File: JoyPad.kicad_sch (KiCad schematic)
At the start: 0 parts

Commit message: Adding the MCU, OLED Screen, Rotary Encoder, and switches to the sch (not done)
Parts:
- added D1, D2, D3, D4, D5, D6: (no value), symbol ScottoKeebs:Placeholder_Diode
- added J1: OLED_128x32, ScottoKeebs_Components:OLED_128x32, symbol ScottoKeebs:OLED_128x32
- added S1, S2, S3, S4, S5, S6: (no value), symbol ScottoKeebs:Placeholder_Keyswitch
- added SW1: RotaryEncoder_Switch, symbol Device:RotaryEncoder_Switch
- added U1: MCU_Seeed_XIAO_RP2040, symbol ScottoKeebs:MCU_Seeed_XIAO_RP2040
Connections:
- new net: D2.2 (A), S2.2
- new net: D6.2 (A), S6.2
- new net: D5.2 (A), S5.2
- new net: D3.2 (A), S3.2
- new net: D4.2 (A), S4.2
- new net: D1.2 (A), S1.2
- new net 5V: J1.2 (VCC), U1.14 (5V)
- new net Col 0: S1.1, S4.1, U1.3 (PA10_A2_D2)
- new net Col 1: S2.1, S5.1, U1.4 (PA11_A3_D3)
- new net Col 2: S3.1, S6.1, U1.11 (PA6_A10_D10_MOSI)
- new net GND: J1.1 (GND), SW1.C, U1.13 (GND)
- new net RNA: SW1.A, U1.9 (PA7_A8_D8_SCK)
- new net RNB: SW1.B, U1.8 (PB09_A7_D7_RX)
- new net RNSWA: SW1.S2
- new net RNSWB: SW1.S1
- new net Row 0: D1.1 (K), D2.1 (K), D3.1 (K), U1.1 (PA02_A0_D0)
- new net Row 2: D4.1 (K), D5.1 (K), D6.1 (K), U1.2 (PA4_A1_D1)
- new net SCL: J1.3 (SCL), U1.6 (PA9_A5_D5_SCL)
- new net SDA: J1.4 (SDA), U1.5 (PA8_A4_D4_SDA)

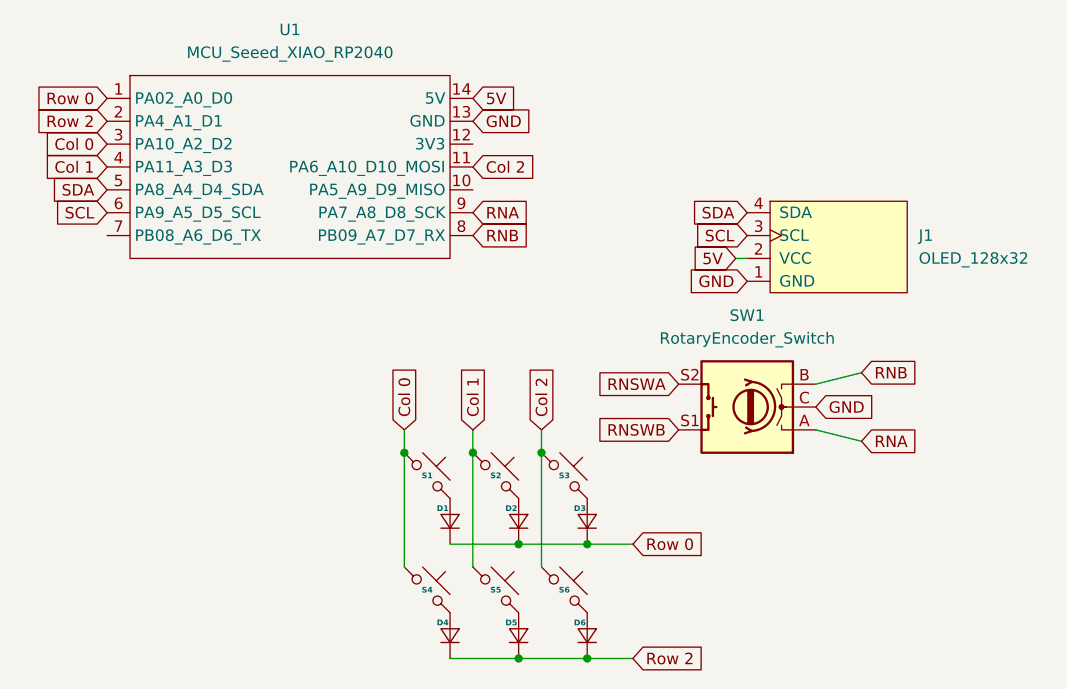
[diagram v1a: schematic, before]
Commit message: Created the PCB For the JoyPad
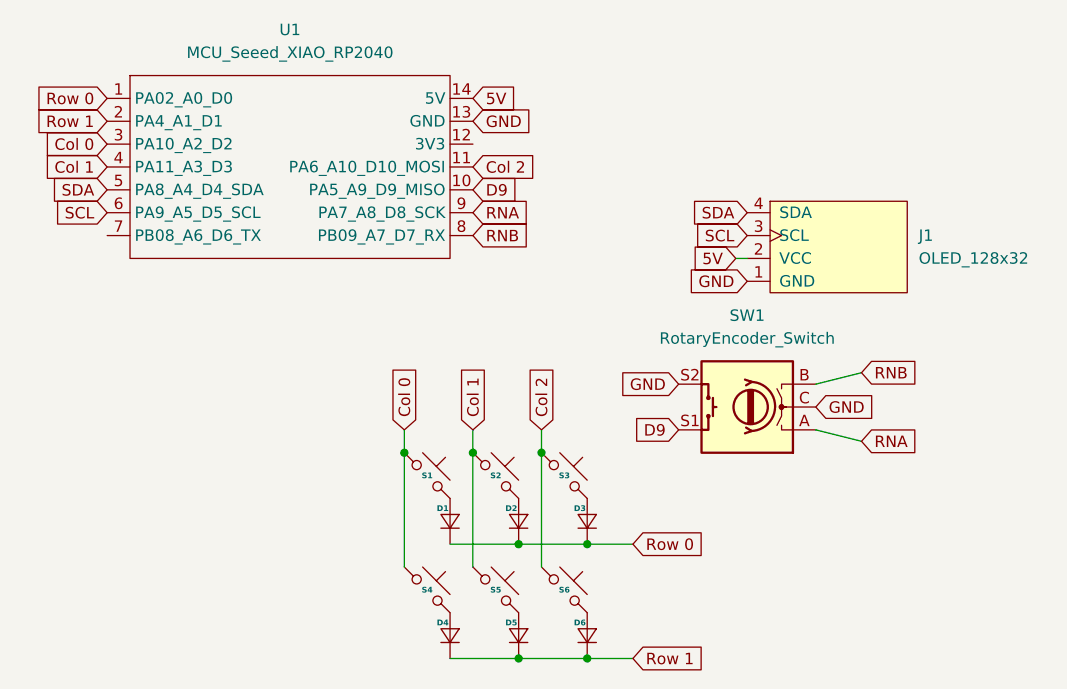
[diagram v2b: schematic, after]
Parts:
- D1, D2, D3, D4, D5, D6: footprint (none) -> ScottoKeebs_Components:Diode_DO-35
- S1, S2, S3, S4, S5, S6: footprint (none) -> ScottoKeebs_Hotswap:Hotswap_MX_1.00u
- SW1: footprint (none) -> Rotary_Encoder:RotaryEncoder_Alps_EC11E-Switch_Vertical_H20mm
- U1: footprint (none) -> ScottoKeebs_MCU:Seeed_XIAO_RP2040
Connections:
- net RNSWA is gone; now on net GND: SW1.S2
- net RNSWB is gone; now on net D9: SW1.S1
- net D9: now reaches U1.10 (PA5_A9_D9_MISO)
- net Row 2 renamed Row 1
